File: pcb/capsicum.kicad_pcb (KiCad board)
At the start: 2 copper layers, 68.6 x 57.7 mm, 74 parts, among them J2 Screw terminal, J3 USB-C 16+8 USB 2.0, Q1 NS2101P, Q2 BC817, SW1 SW_SPDT, SW3 SW_SPDT, U1 ESP32-C3-WROOM-02, U2 TQ33E-1, U3 AP2112K, U4 MCP73831

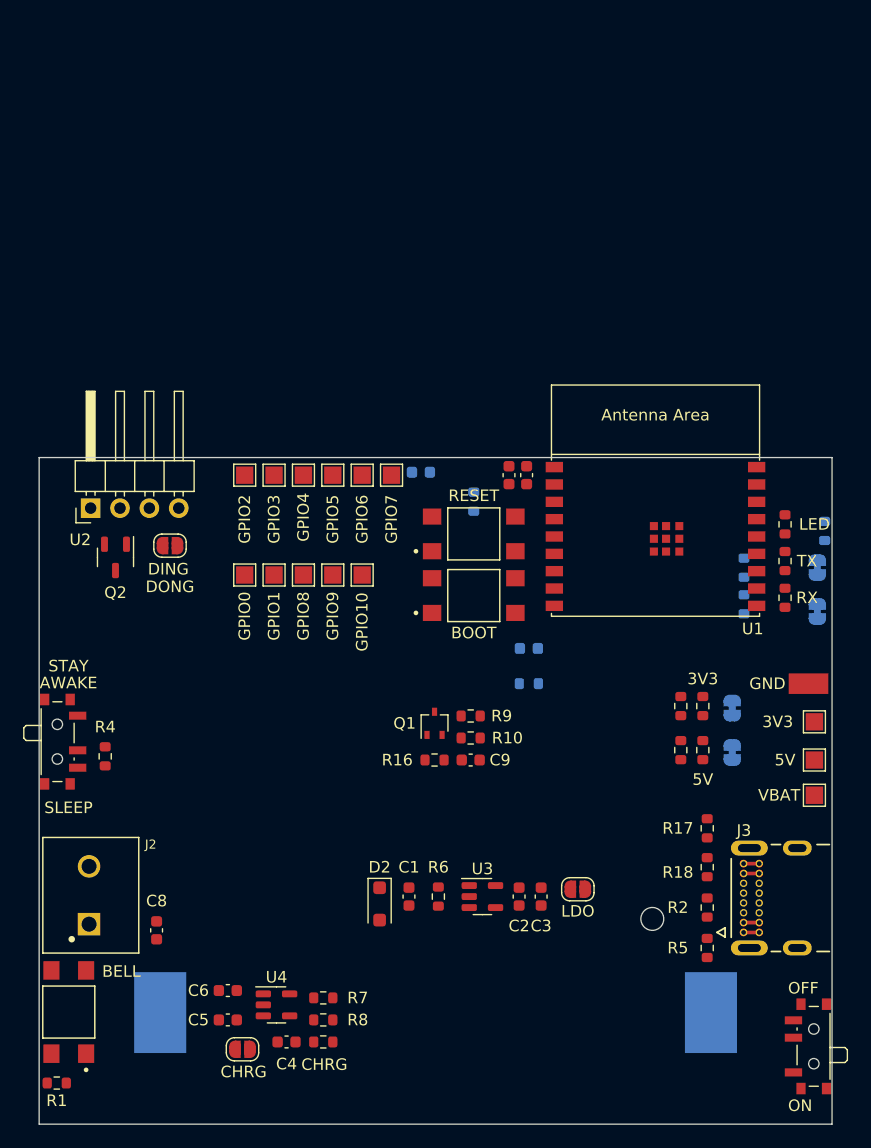
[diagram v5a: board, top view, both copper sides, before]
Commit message: feat: replace 3x open jumpers with solderless option of header pins for jumper caps
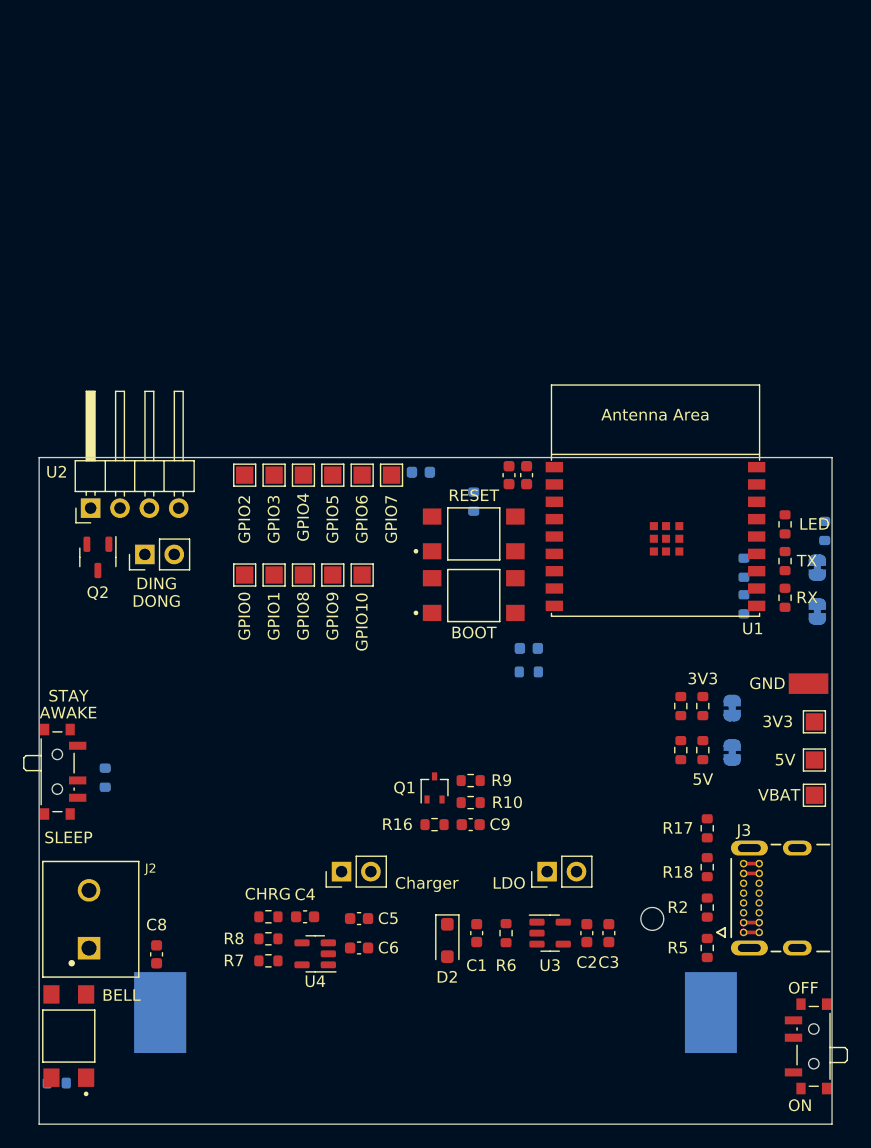
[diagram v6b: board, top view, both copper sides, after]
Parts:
- JP1, JP2, JP3: footprint Jumper:SolderJumper-2_P1.3mm_Open_RoundedPad1.0x1.5mm -> Connector_PinHeader_2.54mm:PinHeader_1x02_P2.54mm_Vertical
- R1, R4: moved to B.Cu
- moved JP2 17.6 mm to (130.3, 117.9), turned to 90 degrees
- moved C5 14.3 mm to (131.8, 121.9), turned to 0 degrees
- moved C6 11.9 mm to (131.8, 124.5), turned to 0 degrees
- moved D3 11.8 mm to (124.0, 121.8), turned to 0 degrees
- moved C4 10.9 mm to (127.1, 121.8), turned to 0 degrees
- moved R8 8.47 mm to (124.0, 123.7), turned to 180 degrees
- moved C1 6.66 mm to (142.0, 123.2)
- moved C2 6.66 mm to (151.5, 123.2)
- moved C3 6.66 mm to (153.4, 123.2)
- moved R6 6.66 mm to (144.5, 123.2)
- moved U3 6.66 mm to (148.3, 123.2)
- moved D2 6.66 mm to (139.4, 123.8)
- moved R7 5.73 mm to (124.0, 125.6), turned to 0 degrees
- moved C9 5.59 mm to (141.5, 113.8)
- moved Q1 5.59 mm to (138.3, 110.6)
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
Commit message: refactor: put all LEDs together and shorten the board
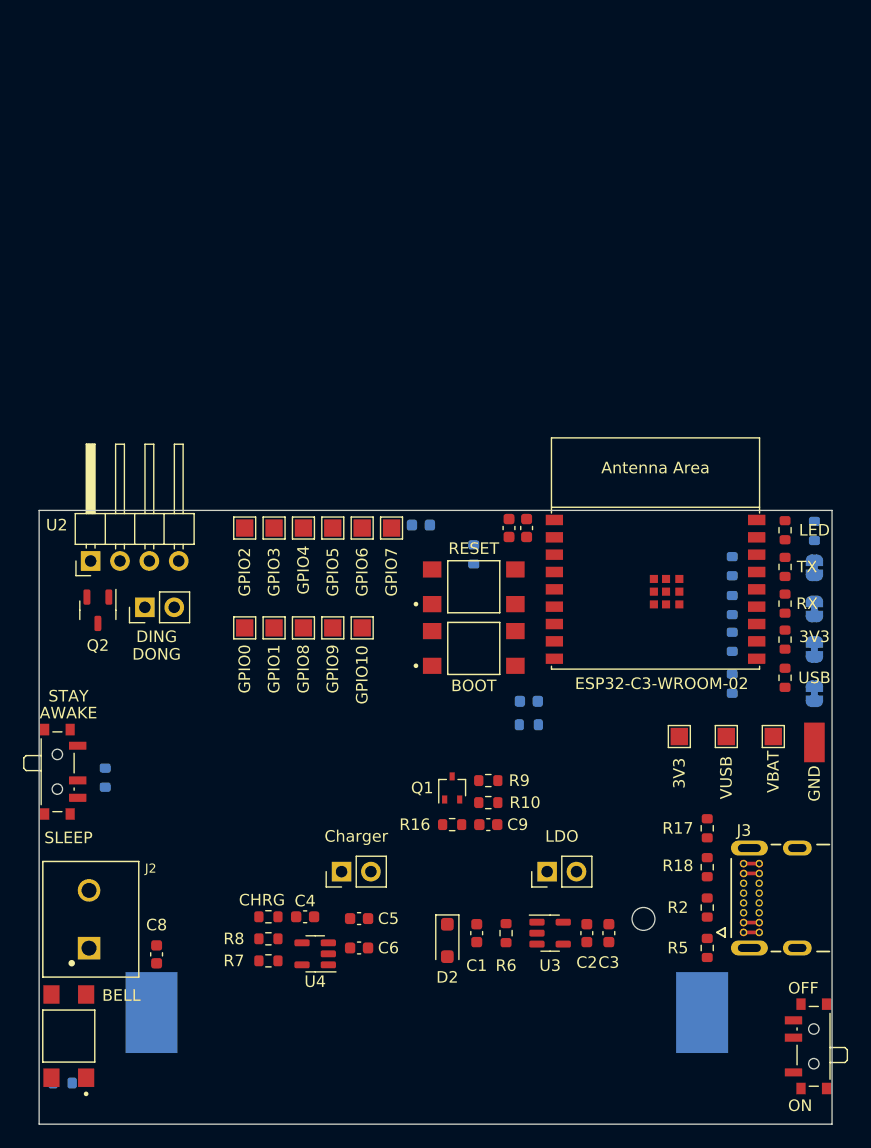
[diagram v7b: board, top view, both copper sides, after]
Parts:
- R14, R15: moved to B.Cu
- moved TP3 11.8 mm to (159.5, 106.2), turned to 90 degrees
- moved D6 9.47 mm to (168.7, 101.1)
- moved D7 9.15 mm to (168.7, 97.8)
- moved JP4 8.74 mm to (171.2, 102.5)
- moved JP5 8.74 mm to (171.2, 98.6)
- moved TP1 7.89 mm to (163.6, 106.2), turned to 90 degrees
- moved R14 7.27 mm to (164.1, 101.6)
- moved R15 7.12 mm to (164.1, 98.0)
- moved TP2 6.20 mm to (167.6, 106.2), turned to 90 degrees
- moved TP15 5.11 mm to (171.2, 106.7), turned to 90 degrees
- moved C10 4.57 mm to (146.3, 88.1)
- moved C11 4.57 mm to (144.8, 88.1)
- moved C7 4.57 mm to (137.2, 87.9)
- moved Q2 4.57 mm to (109.2, 95.2)
- moved R13 4.57 mm to (141.7, 90.4)
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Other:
- board size 68.6 x 57.7 mm -> 68.6 x 53.1 mm

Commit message: feat: add silkscreen text about project
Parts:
- added ?: , clipboard:c3cd3300-634d-4bf5-8c9c-89badbd0db8c, B.Cu at (122.8, 105.4)
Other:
- board text added: "locked"
